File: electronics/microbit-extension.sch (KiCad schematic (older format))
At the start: 1 part

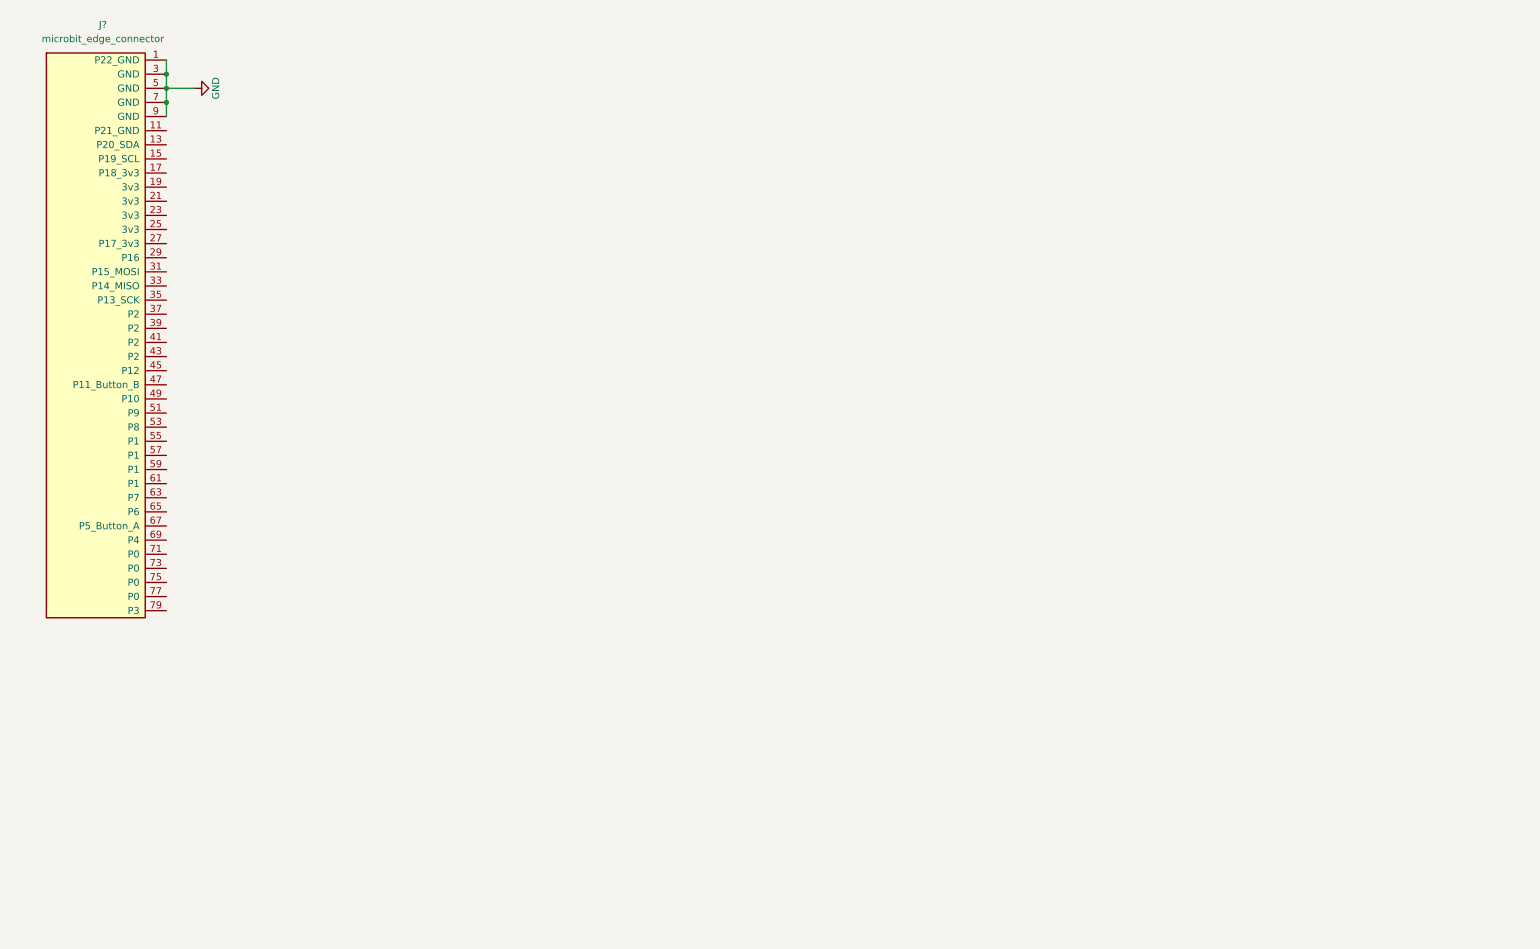
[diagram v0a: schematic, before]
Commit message: schematics for buttons, LEDs and pot
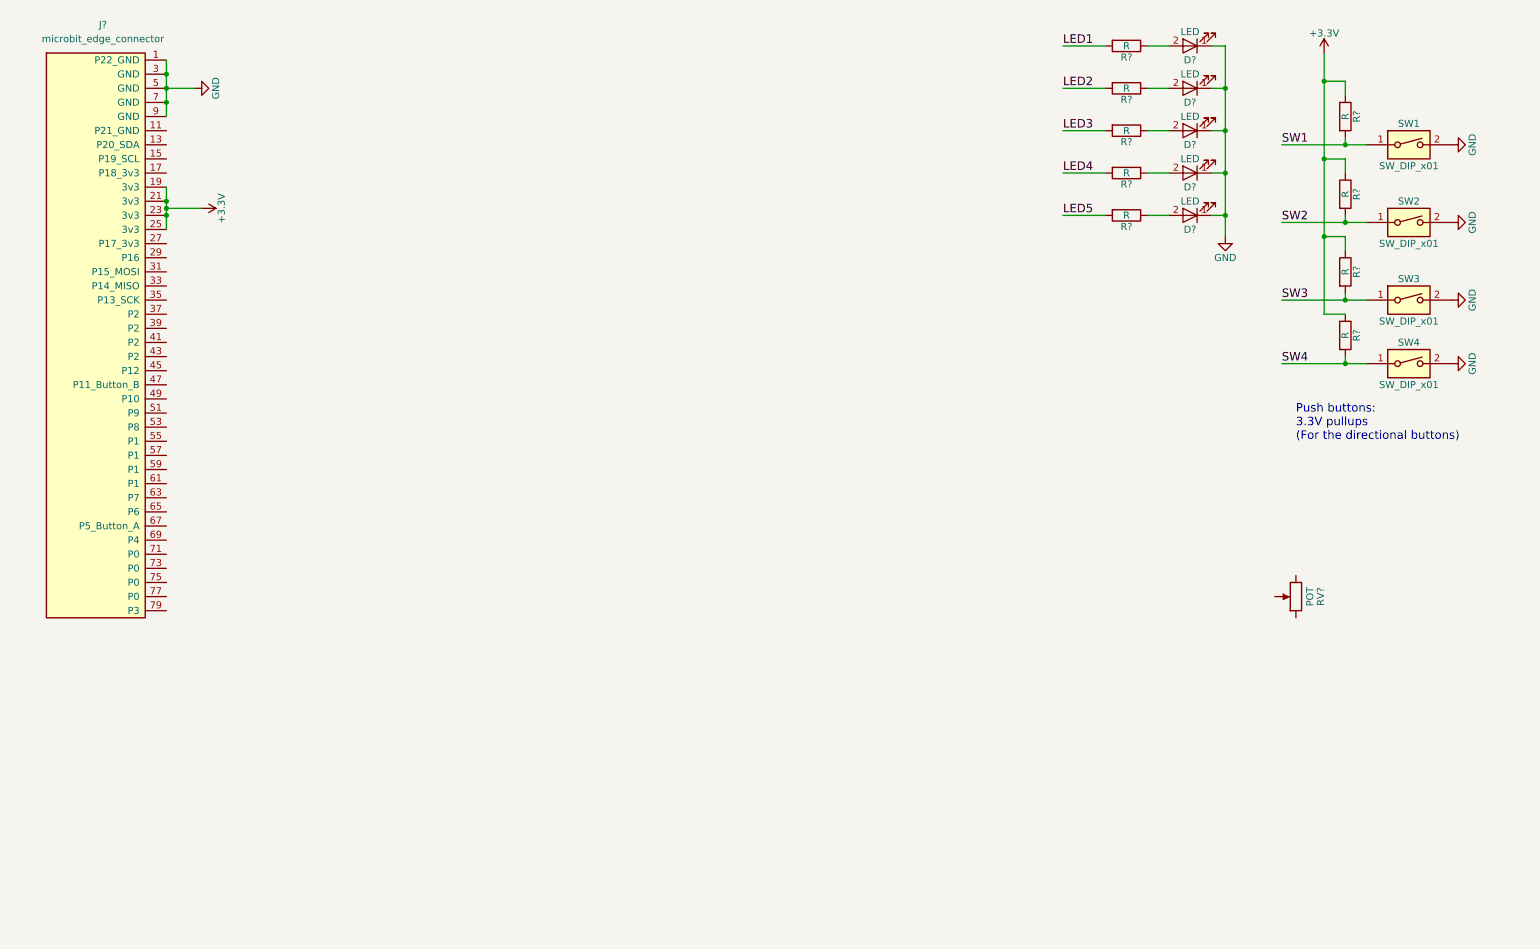
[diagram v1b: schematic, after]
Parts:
- added D? (x5): LED, symbol LED
- added R? (x9): R, symbol R
- added RV?: POT, symbol POT
- added SW1, SW2, SW3, SW4: SW_DIP_x01, symbol SW_DIP_x01
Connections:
- net GND: now also D?.1 (K), D?.1 (K), D?.1 (K), D?.1 (K), D?.1 (K), SW1.2, SW2.2, SW3.2, SW4.2
- net +3V3: now reaches J?.19 (3v3)
- net +3V3: now also J?.21 (3v3), J?.23 (3v3), J?.25 (3v3), R?.1, R?.1, R?.1, R?.1
- new net: D?.2 (A), R?.1 (x5)
- new net LED1: R?.2
- new net LED2: R?.2
- new net LED3: R?.2
- new net LED4: R?.2
- new net LED5: R?.2
- new net SW1: R?.2, SW1.1
- new net SW2: R?.2, SW2.1
- new net SW3: R?.2, SW3.1
- new net SW4: R?.2, SW4.1
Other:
- note added: "Push buttons:\n3.3V pullups\n(For the directional buttons)"

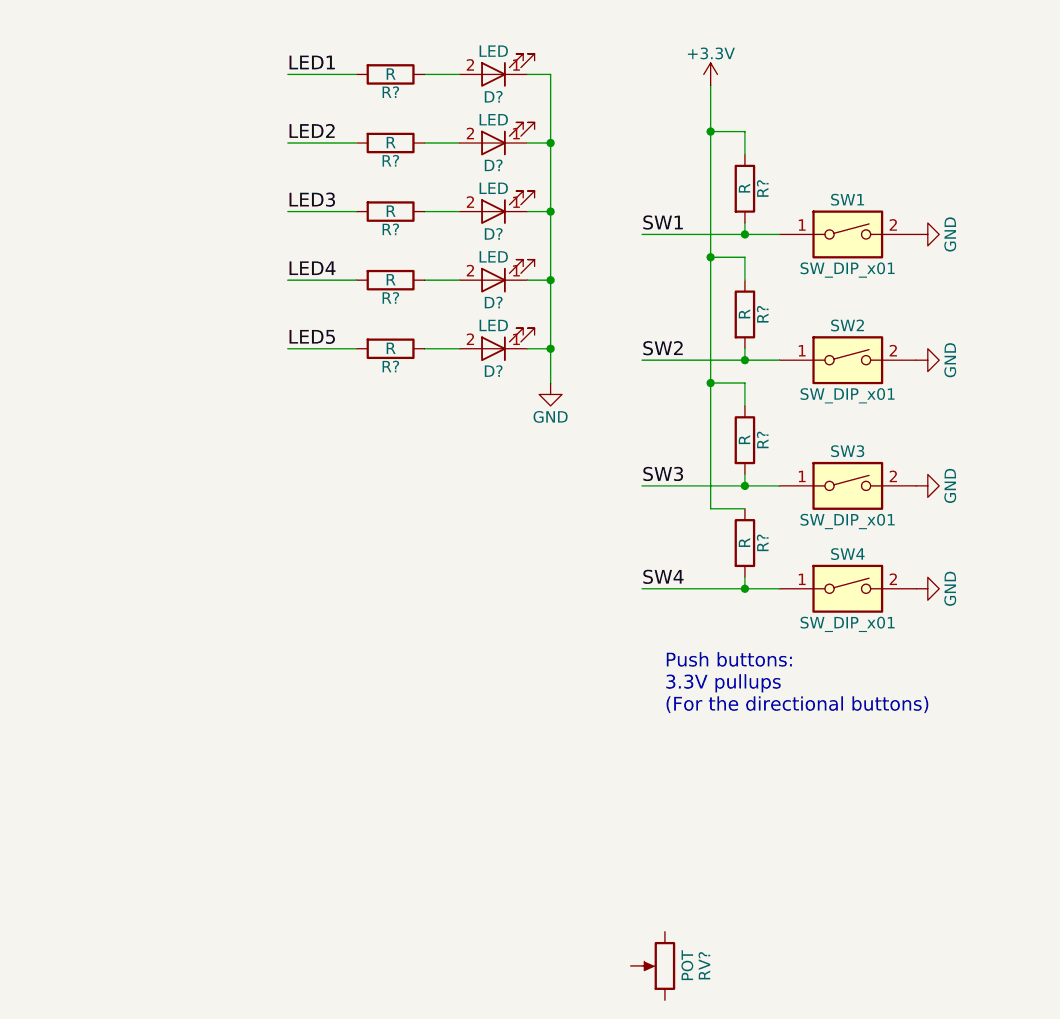
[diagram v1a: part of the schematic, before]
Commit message: some notes on power consumption
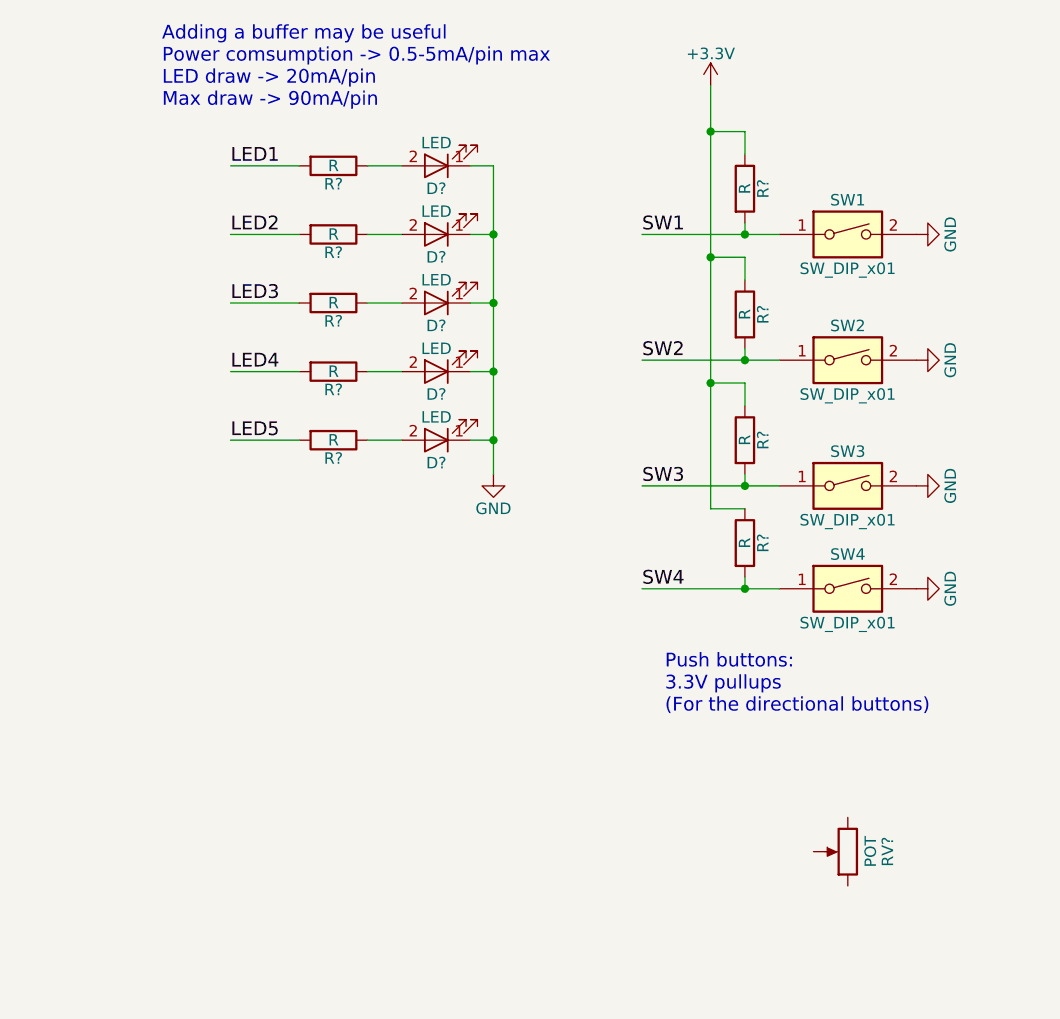
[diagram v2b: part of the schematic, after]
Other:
- note added: "Adding a buffer may be useful\nPower comsumption -> 0.5-5mA/pin max\nLED draw -> 20mA/pin\nMax draw -> 90mA/pin\n"
- moved on the sheet: D?, R?, RV?
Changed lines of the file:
@@
 L POT RV?
 U 1 1 598596E1
-P 9800 4650
-F 0 "RV?" V 9625 4650 50  0000 C CNN
-F 1 "POT" V 9700 4650 50  0000 C CNN
-F 2 "" H 9800 4650 50  0001 C CNN
-F 3 "" H 9800 4650 50  0001 C CNN
-	1    9800 4650
+P 10600 4150
+F 0 "RV?" V 10425 4150 50  0000 C CNN
+F 1 "POT" V 10500 4150 50  0000 C CNN
+F 2 "" H 10600 4150 50  0001 C CNN
+F 3 "" H 10600 4150 50  0001 C CNN
+	1    10600 4150
 	-1   0    0    1
 $EndComp
@@
 L LED D?
 U 1 1 598598B8
-P 9050 750
-F 0 "D?" H 9050 850 50  0000 C CNN
-F 1 "LED" H 9050 650 50  0000 C CNN
-F 2 "" H 9050 750 50  0001 C CNN
-F 3 "" H 9050 750 50  0001 C CNN
-	1    9050 750
+P 8800 1150
+F 0 "D?" H 8800 1250 50  0000 C CNN
+F 1 "LED" H 8800 1050 50  0000 C CNN
+F 2 "" H 8800 1150 50  0001 C CNN
+F 3 "" H 8800 1150 50  0001 C CNN
+	1    8800 1150
 	-1   0    0    1
 $EndComp
@@
 L R R?
 U 1 1 59859901
-P 8600 750
-F 0 "R?" V 8680 750 50  0000 C CNN
-F 1 "R" V 8600 750 50  0000 C CNN
-F 2 "" V 8530 750 50  0001 C CNN
-F 3 "" H 8600 750 50  0001 C CNN
-	1    8600 750
-	0    1    1    0
-$EndComp
-Text Label 8150 750  0    60   ~ 0
+P 8350 1150
+F 0 "R?" V 8430 1150 50  0000 C CNN
+F 1 "R" V 8350 1150 50  0000 C CNN
+F 2 "" V 8280 1150 50  0001 C CNN
+F 3 "" H 8350 1150 50  0001 C CNN
+	1    8350 1150
+	0    1    1    0
+$EndComp
+Text Label 7900 1150 0    60   ~ 0
 LED1
 $Comp
 L LED D?
 U 1 1 59859B13
-P 9050 1350
-F 0 "D?" H 9050 1450 50  0000 C CNN
-F 1 "LED" H 9050 1250 50  0000 C CNN
-F 2 "" H 9050 1350 50  0001 C CNN
-F 3 "" H 9050 1350 50  0001 C CNN
-	1    9050 1350
+P 8800 1750
+F 0 "D?" H 8800 1850 50  0000 C CNN
+F 1 "LED" H 8800 1650 50  0000 C CNN
+F 2 "" H 8800 1750 50  0001 C CNN
+F 3 "" H 8800 1750 50  0001 C CNN
+	1    8800 1750
 	-1   0    0    1
 $EndComp
@@
 L R R?
 U 1 1 59859B19
-P 8600 1350
-F 0 "R?" V 8680 1350 50  0000 C CNN
-F 1 "R" V 8600 1350 50  0000 C CNN
-F 2 "" V 8530 1350 50  0001 C CNN
-F 3 "" H 8600 1350 50  0001 C CNN
-	1    8600 1350
-	0    1    1    0
-$EndComp
-Text Label 8150 1350 0    60   ~ 0
+P 8350 1750
+F 0 "R?" V 8430 1750 50  0000 C CNN
+F 1 "R" V 8350 1750 50  0000 C CNN
+F 2 "" V 8280 1750 50  0001 C CNN
+F 3 "" H 8350 1750 50  0001 C CNN
+	1    8350 1750
+	0    1    1    0
+$EndComp
+Text Label 7900 1750 0    60   ~ 0
 LED3
 $Comp
 L LED D?
 U 1 1 59859BF9
-P 9050 1050
-F 0 "D?" H 9050 1150 50  0000 C CNN
-F 1 "LED" H 9050 950 50  0000 C CNN
-F 2 "" H 9050 1050 50  0001 C CNN
-F 3 "" H 9050 1050 50  0001 C CNN
-	1    9050 1050
+P 8800 1450
+F 0 "D?" H 8800 1550 50  0000 C CNN
+F 1 "LED" H 8800 1350 50  0000 C CNN
+F 2 "" H 8800 1450 50  0001 C CNN
+F 3 "" H 8800 1450 50  0001 C CNN
+	1    8800 1450
 	-1   0    0    1
 $EndComp
@@
 L R R?
 U 1 1 59859BFF
-P 8600 1050
-F 0 "R?" V 8680 1050 50  0000 C CNN
-F 1 "R" V 8600 1050 50  0000 C CNN
-F 2 "" V 8530 1050 50  0001 C CNN
-F 3 "" H 8600 1050 50  0001 C CNN
-	1    8600 1050
-	0    1    1    0
-$EndComp
-Text Label 8150 1050 0    60   ~ 0
+P 8350 1450
+F 0 "R?" V 8430 1450 50  0000 C CNN
+F 1 "R" V 8350 1450 50  0000 C CNN
+F 2 "" V 8280 1450 50  0001 C CNN
+F 3 "" H 8350 1450 50  0001 C CNN
+	1    8350 1450
+	0    1    1    0
+$EndComp
+Text Label 7900 1450 0    60   ~ 0
 LED2
 $Comp
 L LED D?
 U 1 1 59859C45
-P 9050 1650
-F 0 "D?" H 9050 1750 50  0000 C CNN
-F 1 "LED" H 9050 1550 50  0000 C CNN
-F 2 "" H 9050 1650 50  0001 C CNN
-F 3 "" H 9050 1650 50  0001 C CNN
-	1    9050 1650
+P 8800 2050
+F 0 "D?" H 8800 2150 50  0000 C CNN
+F 1 "LED" H 8800 1950 50  0000 C CNN
+F 2 "" H 8800 2050 50  0001 C CNN
+F 3 "" H 8800 2050 50  0001 C CNN
+	1    8800 2050
 	-1   0    0    1
 $EndComp
@@
 L R R?
 U 1 1 59859C4B
-P 8600 1650
-F 0 "R?" V 8680 1650 50  0000 C CNN
-F 1 "R" V 8600 1650 50  0000 C CNN
-F 2 "" V 8530 1650 50  0001 C CNN
-F 3 "" H 8600 1650 50  0001 C CNN
-	1    8600 1650
-	0    1    1    0
-$EndComp
-Text Label 8150 1650 0    60   ~ 0
+P 8350 2050
+F 0 "R?" V 8430 2050 50  0000 C CNN
+F 1 "R" V 8350 2050 50  0000 C CNN
+F 2 "" V 8280 2050 50  0001 C CNN
+F 3 "" H 8350 2050 50  0001 C CNN
+	1    8350 2050
+	0    1    1    0
+$EndComp
+Text Label 7900 2050 0    60   ~ 0
 LED4
 $Comp
 L LED D?
 U 1 1 59859C97
-P 9050 1950
-F 0 "D?" H 9050 2050 50  0000 C CNN
-F 1 "LED" H 9050 1850 50  0000 C CNN
-F 2 "" H 9050 1950 50  0001 C CNN
-F 3 "" H 9050 1950 50  0001 C CNN
-	1    9050 1950
+P 8800 2350
+F 0 "D?" H 8800 2450 50  0000 C CNN
+F 1 "LED" H 8800 2250 50  0000 C CNN
+F 2 "" H 8800 2350 50  0001 C CNN
+F 3 "" H 8800 2350 50  0001 C CNN
+	1    8800 2350
 	-1   0    0    1
 $EndComp
@@
 L R R?
 U 1 1 59859C9D
-P 8600 1950
-F 0 "R?" V 8680 1950 50  0000 C CNN
-F 1 "R" V 8600 1950 50  0000 C CNN
-F 2 "" V 8530 1950 50  0001 C CNN
-F 3 "" H 8600 1950 50  0001 C CNN
-	1    8600 1950
+P 8350 2350
+F 0 "R?" V 8430 2350 50  0000 C CNN
+F 1 "R" V 8350 2350 50  0000 C CNN
+F 2 "" V 8280 2350 50  0001 C CNN
+F 3 "" H 8350 2350 50  0001 C CNN
+	1    8350 2350
 	0    1    1    0
 $EndComp
@@
 L GND #PWR?
 U 1 1 59859CA3
-P 9300 2100
-F 0 "#PWR?" H 9300 1850 50  0001 C CNN
-F 1 "GND" H 9300 1950 50  0000 C CNN
-F 2 "" H 9300 2100 50  0001 C CNN
-F 3 "" H 9300 2100 50  0001 C CNN
-	1    9300 2100
+P 9050 2500
+F 0 "#PWR?" H 9050 2250 50  0001 C CNN
+F 1 "GND" H 9050 2350 50  0000 C CNN
+F 2 "" H 9050 2500 50  0001 C CNN
+F 3 "" H 9050 2500 50  0001 C CNN
+	1    9050 2500
 	1    0    0    -1
 $EndComp
-Text Label 8150 1950 0    60   ~ 0
+Text Label 7900 2350 0    60   ~ 0
 LED5
 $Comp
@@
 Connection ~ 10000 2100
 Wire Wire Line
-	9200 750  9300 750
-Wire Wire Line
-	8750 750  8900 750
-Wire Wire Line
-	8150 750  8450 750
-Wire Wire Line
-	9300 1350 9200 1350
-Wire Wire Line
-	8750 1350 8900 1350
-Wire Wire Line
-	8150 1350 8450 1350
-Wire Wire Line
-	9200 1050 9300 1050
-Wire Wire Line
-	8750 1050 8900 1050
-Wire Wire Line
-	8150 1050 8450 1050
-Wire Wire Line
-	9300 1650 9200 1650
-Wire Wire Line
-	8750 1650 8900 1650
-Wire Wire Line
-	8150 1650 8450 1650
-Wire Wire Line
-	9300 1950 9200 1950
-Wire Wire Line
-	8750 1950 8900 1950
-Wire Wire Line
-	8150 1950 8450 1950
-Wire Wire Line
-	9300 750  9300 2100
-Connection ~ 9300 1050
-Connection ~ 9300 1350
-Connection ~ 9300 1650
-Connection ~ 9300 1950
+	8950 1150 9050 1150
+Wire Wire Line
+	8500 1150 8650 1150
+Wire Wire Line
+	7900 1150 8200 1150
+Wire Wire Line
+	9050 1750 8950 1750
+Wire Wire Line
+	8500 1750 8650 1750
+Wire Wire Line
+	7900 1750 8200 1750
+Wire Wire Line
+	8950 1450 9050 1450
+Wire Wire Line
+	8500 1450 8650 1450
+Wire Wire Line
+	7900 1450 8200 1450
+Wire Wire Line
+	9050 2050 8950 2050
+Wire Wire Line
+	8500 2050 8650 2050
+Wire Wire Line
+	7900 2050 8200 2050
+Wire Wire Line
+	9050 2350 8950 2350
+Wire Wire Line
+	8500 2350 8650 2350
+Wire Wire Line
+	7900 2350 8200 2350
+Wire Wire Line
+	9050 1150 9050 2500
+Connection ~ 9050 1450
+Connection ~ 9050 1750
+Connection ~ 9050 2050
+Connection ~ 9050 2350
 Wire Wire Line
 	1800 1750 1800 2050
@@
 	2050 1900 1800 1900
 Connection ~ 1800 1900
+Text Notes 7600 900  0    60   ~ 0
+Adding a buffer may be useful\nPower comsumption -> 0.5-5mA/pin max\nLED draw -> 20mA/pin\nMax draw -> 90mA/pin\n
 $EndSCHEMATC
